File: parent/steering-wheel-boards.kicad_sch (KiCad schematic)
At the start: 74 parts, among them J1 Conn_01x08, J2 Conn_01x06, J3 Conn_01x06, J4 Conn_01x04, Q1 2N2222A, Q2 2N2222A, U3 TLC5951DAP, U4 LT1117-5.0, U5 MCP2561-E-SN

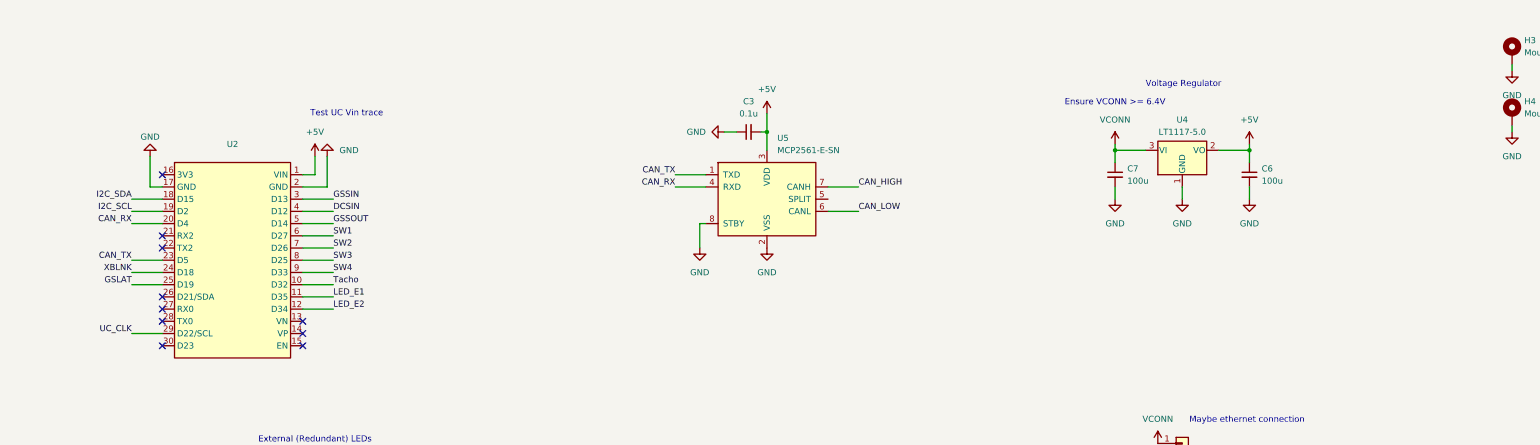
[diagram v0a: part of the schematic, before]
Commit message: Replace ESP32 with RP2350 Zero
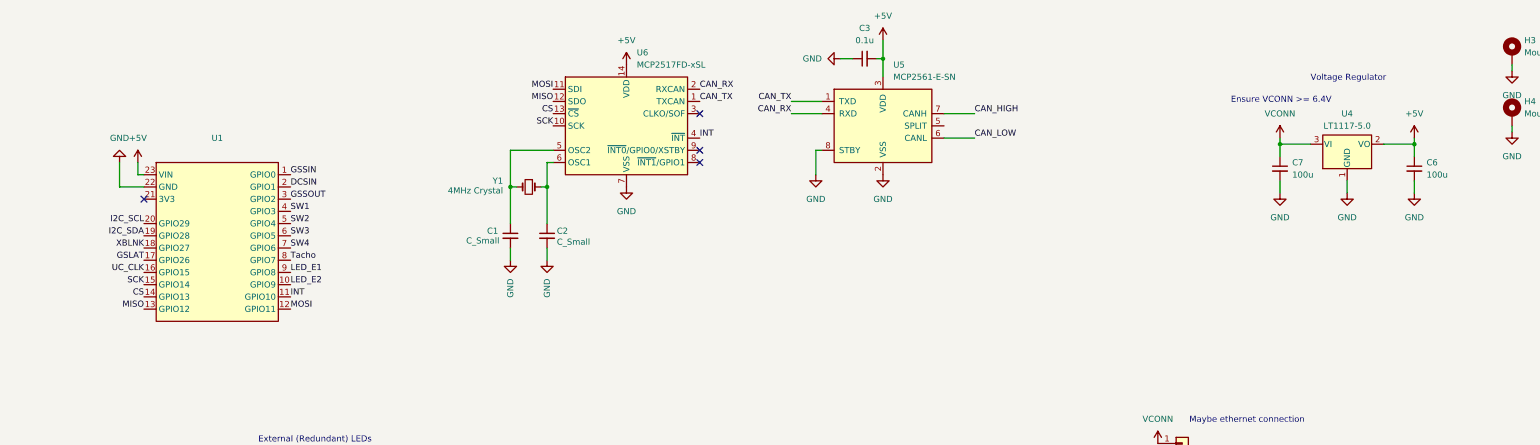
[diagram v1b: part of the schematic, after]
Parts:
- removed U2: ~, FBR_Footprints:ESP32_30pin, symbol FBR_Symbols:ESP32-BOB-FBR26
- added C1, C2: C_Small, symbol Device:C_Small
- added U1: ~, symbol FBR_MCU:MCU_RP2350_Zero
- added U6: MCP2517FD-xSL, Package_SO:SOIC-14_3.9x8.7mm_P1.27mm, symbol Interface_CAN_LIN:MCP2517FD-xSL
- added Y1: 4MHz Crystal, symbol Device:Crystal_Small
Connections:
- net +5V: now also U1.23 (VIN), U6.14 (VDD)
- net CAN_RX: now also U6.2 (RXCAN)
- net CAN_TX: now also U6.1 (TXCAN)
- net DCSIN: now also U1.2 (GPIO1)
- net GND: now also C1.2, C2.2, U1.22 (GND), U6.7 (VSS)
- net GSLAT: now also U1.17 (GPIO26)
- net GSSIN: now also U1.1 (GPIO0)
- net GSSOUT: now also U1.3 (GPIO2)
- net I2C_SCL: now also U1.20 (GPIO29)
- net I2C_SDA: now also U1.19 (GPIO28)
- net LED_E1: now also U1.9 (GPIO8)
- net LED_E2: now also U1.10 (GPIO9)
- net SW1: now also U1.4 (GPIO3)
- net SW2: now also U1.5 (GPIO4)
- net SW3: now also U1.6 (GPIO5)
- net SW4: now also U1.7 (GPIO6)
- net Tacho: now also U1.8 (GPIO7)
- net UC_CLK: now also U1.16 (GPIO15)
- net XBLNK: now also U1.18 (GPIO27)
- new net: C2.1, U6.6 (OSC1), Y1.1
- new net: C1.1, U6.5 (OSC2), Y1.2
- new net CS: U1.14 (GPIO13), U6.13 (~{CS})
- new net INT: U1.11 (GPIO10), U6.4 (~{INT})
- new net MISO: U1.13 (GPIO12), U6.12 (SDO)
- new net MOSI: U1.12 (GPIO11), U6.11 (SDI)
- new net SCK: U1.15 (GPIO14), U6.10 (SCK)
- no-connect marks 13 -> 7
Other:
- note removed: "Test UC Vin trace"
- moved on the sheet: C3, C6, C7, U4, U5

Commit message: Assign footprints
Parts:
- C1, C2: value C_Small -> 32p; footprint (none) -> SteeringWheel:CAP_RCER72A105K2DBH03A
- C3, C4, C5: footprint FBR_Footprints:CAP_RCER72A105K2DBH03A -> SteeringWheel:CAP_RCER72A105K2DBH03A
- C6: footprint (none) -> SteeringWheel:CAP_RCER72A105K2DBH03A
- C7: value 100u -> 10u; footprint (none) -> SteeringWheel:CAP_RCER72A105K2DBH03A
- D1, D10, D11, D12, D13, D14, D15, D16, D17, D18, D19, D2, D20, D21, D22, D23, D24, D26, D27, D3, D4, D5, D6, D7, D8, D9: footprint FBR_Footprints:5990K80107F -> SteeringWheel:5990K80107F
- Q1, Q2: footprint FBR_Footprints:2N2222A -> SteeringWheel:2N2222A
- U1: footprint (none) -> SteeringWheel:RP2350_Zero
- U4: footprint (none) -> Package_TO_SOT_SMD:SOT-223
- Y1: value 4MHz Crystal -> ABM7-20.000MHZ-D2Y-T; footprint (none) -> Crystal:Crystal_SMD_Abracon_ABM7-2Pin_6.0x3.5mm
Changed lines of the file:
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@@
 			)
 		)
-		(property "Footprint" ""
+		(property "Footprint" "SteeringWheel:CAP_RCER72A105K2DBH03A"
 			(at 328.93 55.88 0)
 			(effects
@@
 			)
 		)
-		(property "Footprint" ""
+		(property "Footprint" "Package_TO_SOT_SMD:SOT-223"
 			(at 314.96 50.8 0)
 			(effects
@@
 			)
 		)
-		(property "Value" "C_Small"
+		(property "Value" "32p"
 			(at 150.622 71.12 0)
 			(effects
@@
 			)
 		)
-		(property "Footprint" ""
+		(property "Footprint" "SteeringWheel:CAP_RCER72A105K2DBH03A"
 			(at 148.59 69.85 0)
 			(effects
@@
 			)
 		)
-		(property "Footprint" "FBR_Footprints:5990K80107F"
+		(property "Footprint" "SteeringWheel:5990K80107F"
 			(at 111.76 187.96 90)
 			(effects
@@
 			)
 		)
-		(property "Footprint" "FBR_Footprints:5990K80107F"
+		(property "Footprint" "SteeringWheel:5990K80107F"
 			(at 172.72 187.96 90)
 			(effects
@@
 			)
 		)
-		(property "Value" "100u"
+		(property "Value" "10u"
 			(at 303.53 57.1562 0)
 			(effects
@@
 			)
 		)
-		(property "Footprint" ""
+		(property "Footprint" "SteeringWheel:CAP_RCER72A105K2DBH03A"
 			(at 300.99 55.88 0)
 			(effects
@@
 			)
 		)
-		(property "Footprint" "FBR_Footprints:5990K80107F"
+		(property "Footprint" "SteeringWheel:5990K80107F"
 			(at 187.96 187.96 90)
 			(effects
@@
 			)
 		)
-		(property "Footprint" "FBR_Footprints:CAP_RCER72A105K2DBH03A"
+		(property "Footprint" "SteeringWheel:CAP_RCER72A105K2DBH03A"
 			(at 214.63 33.02 0)
 			(effects
@@
 			)
 		)
-		(property "Footprint" "FBR_Footprints:5990K80107F"
+		(property "Footprint" "SteeringWheel:5990K80107F"
 			(at 78.74 128.27 90)
 			(effects
@@
 			)
 		)
-		(property "Footprint" "FBR_Footprints:5990K80107F"
+		(property "Footprint" "SteeringWheel:5990K80107F"
 			(at 142.24 187.96 90)
 			(effects
@@
 			)
 		)
-		(property "Footprint" "FBR_Footprints:CAP_RCER72A105K2DBH03A"
+		(property "Footprint" "SteeringWheel:CAP_RCER72A105K2DBH03A"
 			(at 240.03 187.96 0)
 			(effects
@@
 			)
 		)
-		(property "Footprint" "FBR_Footprints:5990K80107F"
+		(property "Footprint" "SteeringWheel:5990K80107F"
 			(at 157.48 187.96 90)
 			(effects
@@
 			)
 		)
-		(property "Footprint" "FBR_Footprints:5990K80107F"
+		(property "Footprint" "SteeringWheel:5990K80107F"
 			(at 198.12 187.96 90)
 			(effects
@@
 			)
 		)
-		(property "Footprint" "FBR_Footprints:5990K80107F"
+		(property "Footprint" "SteeringWheel:5990K80107F"
 			(at 152.4 187.96 90)
 			(effects
@@
 			)
 		)
-		(property "Footprint" "FBR_Footprints:5990K80107F"
+		(property "Footprint" "SteeringWheel:5990K80107F"
 			(at 193.04 187.96 90)
 			(effects
@@
 			)
 		)
-		(property "Footprint" "FBR_Footprints:5990K80107F"
+		(property "Footprint" "SteeringWheel:5990K80107F"
 			(at 115.57 128.27 90)
 			(effects
@@
 			)
 		)
-		(property "Footprint" "FBR_Footprints:2N2222A"
+		(property "Footprint" "SteeringWheel:2N2222A"
 			(at 113.03 137.16 0)
 			(effects
@@
 			)
 		)
-		(property "Footprint" "FBR_Footprints:5990K80107F"
+		(property "Footprint" "SteeringWheel:5990K80107F"
 			(at 167.64 187.96 90)
 			(effects
@@
 			)
 		)
-		(property "Footprint" "FBR_Footprints:2N2222A"
+		(property "Footprint" "SteeringWheel:2N2222A"
 			(at 76.2 137.16 0)
 			(effects
@@
 			)
 		)
-		(property "Value" "C_Small"
+		(property "Value" "32p"
 			(at 138.684 70.866 0)
 			(effects
@@
 			)
 		)
-		(property "Footprint" ""
+		(property "Footprint" "SteeringWheel:CAP_RCER72A105K2DBH03A"
 			(at 140.97 69.85 0)
 			(effects
@@
 			)
 		)
-		(property "Footprint" "FBR_Footprints:5990K80107F"
+		(property "Footprint" "SteeringWheel:5990K80107F"
 			(at 101.6 187.96 90)
 			(effects
@@
 			)
 		)
-		(property "Footprint" "FBR_Footprints:5990K80107F"
+		(property "Footprint" "SteeringWheel:5990K80107F"
 			(at 121.92 187.96 90)
 			(effects
@@
 			)
 		)
-		(property "Footprint" "FBR_Footprints:5990K80107F"
+		(property "Footprint" "SteeringWheel:5990K80107F"
 			(at 127 187.96 90)
 			(effects
@@
 			)
 		)
-		(property "Footprint" ""
+		(property "Footprint" "SteeringWheel:RP2350_Zero"
 			(at 80.01 53.34 0)
 			(effects
@@
 			)
 		)
-		(property "Footprint" "FBR_Footprints:5990K80107F"
+		(property "Footprint" "SteeringWheel:5990K80107F"
 			(at 203.2 187.96 90)
 			(effects
@@
 			)
 		)
-		(property "Footprint" "FBR_Footprints:CAP_RCER72A105K2DBH03A"
+		(property "Footprint" "SteeringWheel:CAP_RCER72A105K2DBH03A"
 			(at 232.41 187.96 0)
 			(effects
@@
 			)
 		)
-		(property "Footprint" "FBR_Footprints:5990K80107F"
+		(property "Footprint" "SteeringWheel:5990K80107F"
 			(at 177.8 187.96 90)
 			(effects
@@
 			)
 		)
-		(property "Footprint" "FBR_Footprints:5990K80107F"
+		(property "Footprint" "SteeringWheel:5990K80107F"
 			(at 106.68 187.96 90)
 			(effects
@@
 			)
 		)
-		(property "Footprint" "FBR_Footprints:5990K80107F"
+		(property "Footprint" "SteeringWheel:5990K80107F"
 			(at 213.36 187.96 90)
 			(effects
@@
 			)
 		)
-		(property "Value" "4MHz Crystal"
+		(property "Value" "ABM7-20.000MHZ-D2Y-T"
 			(at 139.446 60.452 0)
 			(effects
@@
 			)
 		)
-		(property "Footprint" ""
+		(property "Footprint" "Crystal:Crystal_SMD_Abracon_ABM7-2Pin_6.0x3.5mm"
 			(at 144.78 59.69 0)
 			(effects
@@
 			)
 		)
-		(property "Footprint" "FBR_Footprints:5990K80107F"
+		(property "Footprint" "SteeringWheel:5990K80107F"
 			(at 132.08 187.96 90)
 			(effects
@@
 			)
 		)
-		(property "Footprint" "FBR_Footprints:5990K80107F"
+		(property "Footprint" "SteeringWheel:5990K80107F"
 			(at 162.56 187.96 90)
 			(effects
@@
 			)
 		)
-		(property "Footprint" "FBR_Footprints:5990K80107F"
+		(property "Footprint" "SteeringWheel:5990K80107F"
 			(at 116.84 187.96 90)
 			(effects
@@
 			)
 		)
-		(property "Footprint" "FBR_Footprints:5990K80107F"
+		(property "Footprint" "SteeringWheel:5990K80107F"
 			(at 223.52 187.96 90)
 			(effects
@@
 			)
 		)
-		(property "Footprint" "FBR_Footprints:5990K80107F"
+		(property "Footprint" "SteeringWheel:5990K80107F"
 			(at 208.28 187.96 90)
 			(effects
@@
 			)
 		)
-		(property "Footprint" "FBR_Footprints:5990K80107F"
+		(property "Footprint" "SteeringWheel:5990K80107F"
 			(at 147.32 187.96 90)
 			(effects
@@
 			)
 		)
-		(property "Footprint" "FBR_Footprints:5990K80107F"
+		(property "Footprint" "SteeringWheel:5990K80107F"
 			(at 218.44 187.96 90)
 			(effects
@@
 			)
 		)
-		(property "Footprint" "FBR_Footprints:5990K80107F"
+		(property "Footprint" "SteeringWheel:5990K80107F"
 			(at 96.52 187.96 90)
 			(effects

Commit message: Route Steering Wheel
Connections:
- no-connect marks 7 -> 8
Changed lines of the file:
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@@
+	)
+	(no_connect
+		(at 231.14 46.99)
 	)
 	(no_connect

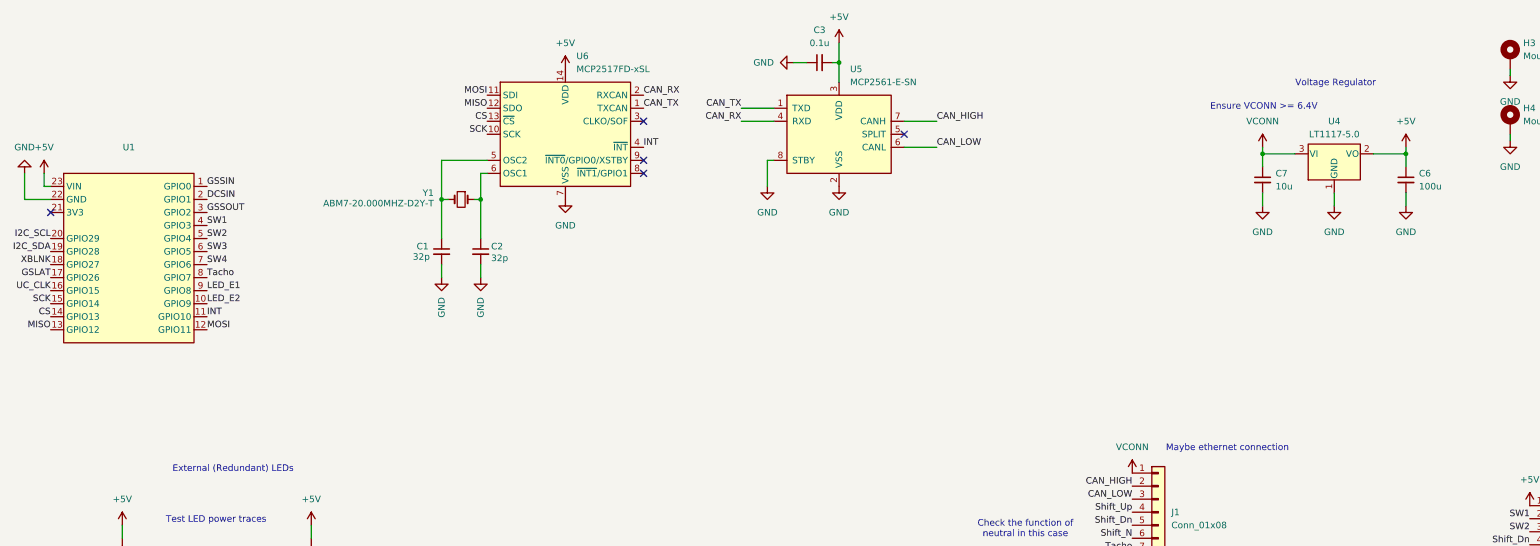
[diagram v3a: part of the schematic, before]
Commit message: Change input voltage to +5V
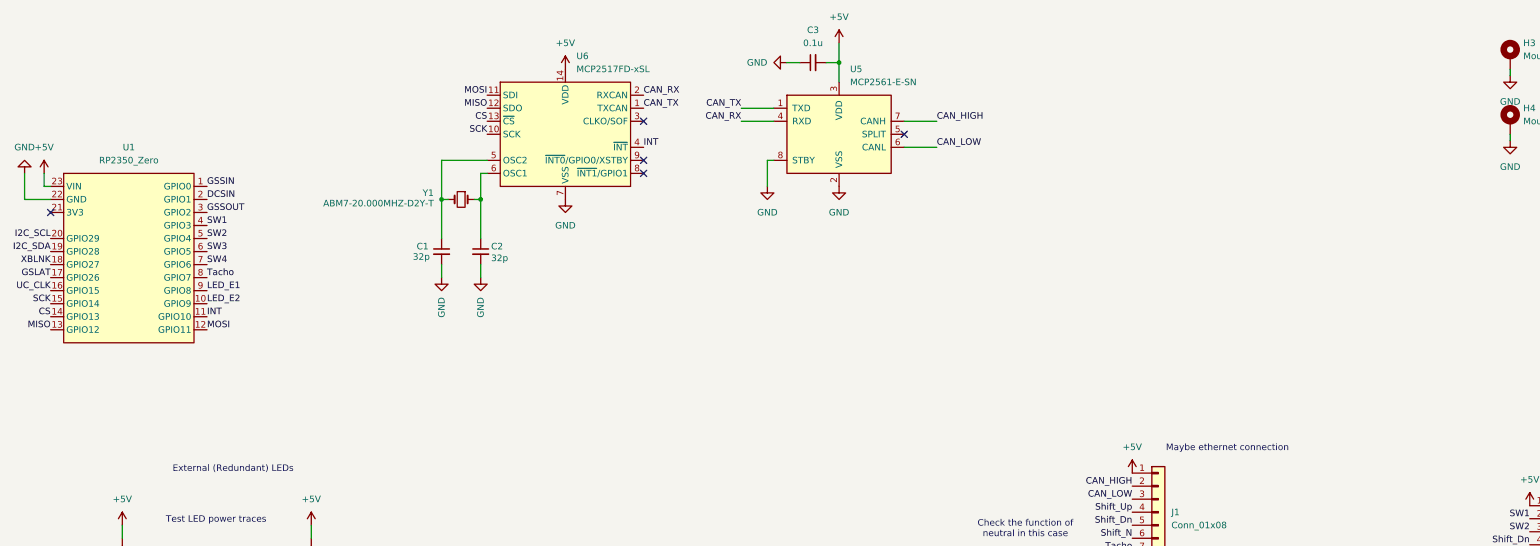
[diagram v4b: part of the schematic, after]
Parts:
- removed C6: 100u, SteeringWheel:CAP_RCER72A105K2DBH03A, symbol Device:C_Small
- removed C7: 10u, SteeringWheel:CAP_RCER72A105K2DBH03A, symbol Device:C_Small
- removed U4: LT1117-5.0, Package_TO_SOT_SMD:SOT-223, symbol Regulator_Linear:LT1117-5.0
- U1: value ~ -> RP2350_Zero
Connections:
- net VCONN is gone; now on net +5V: J1.1 (Pin_1)
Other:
- note removed: "Ensure VCONN >= 6.4V"
- note removed: "Voltage Regulator"
- moved on the sheet: C3
